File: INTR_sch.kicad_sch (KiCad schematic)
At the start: 1 part

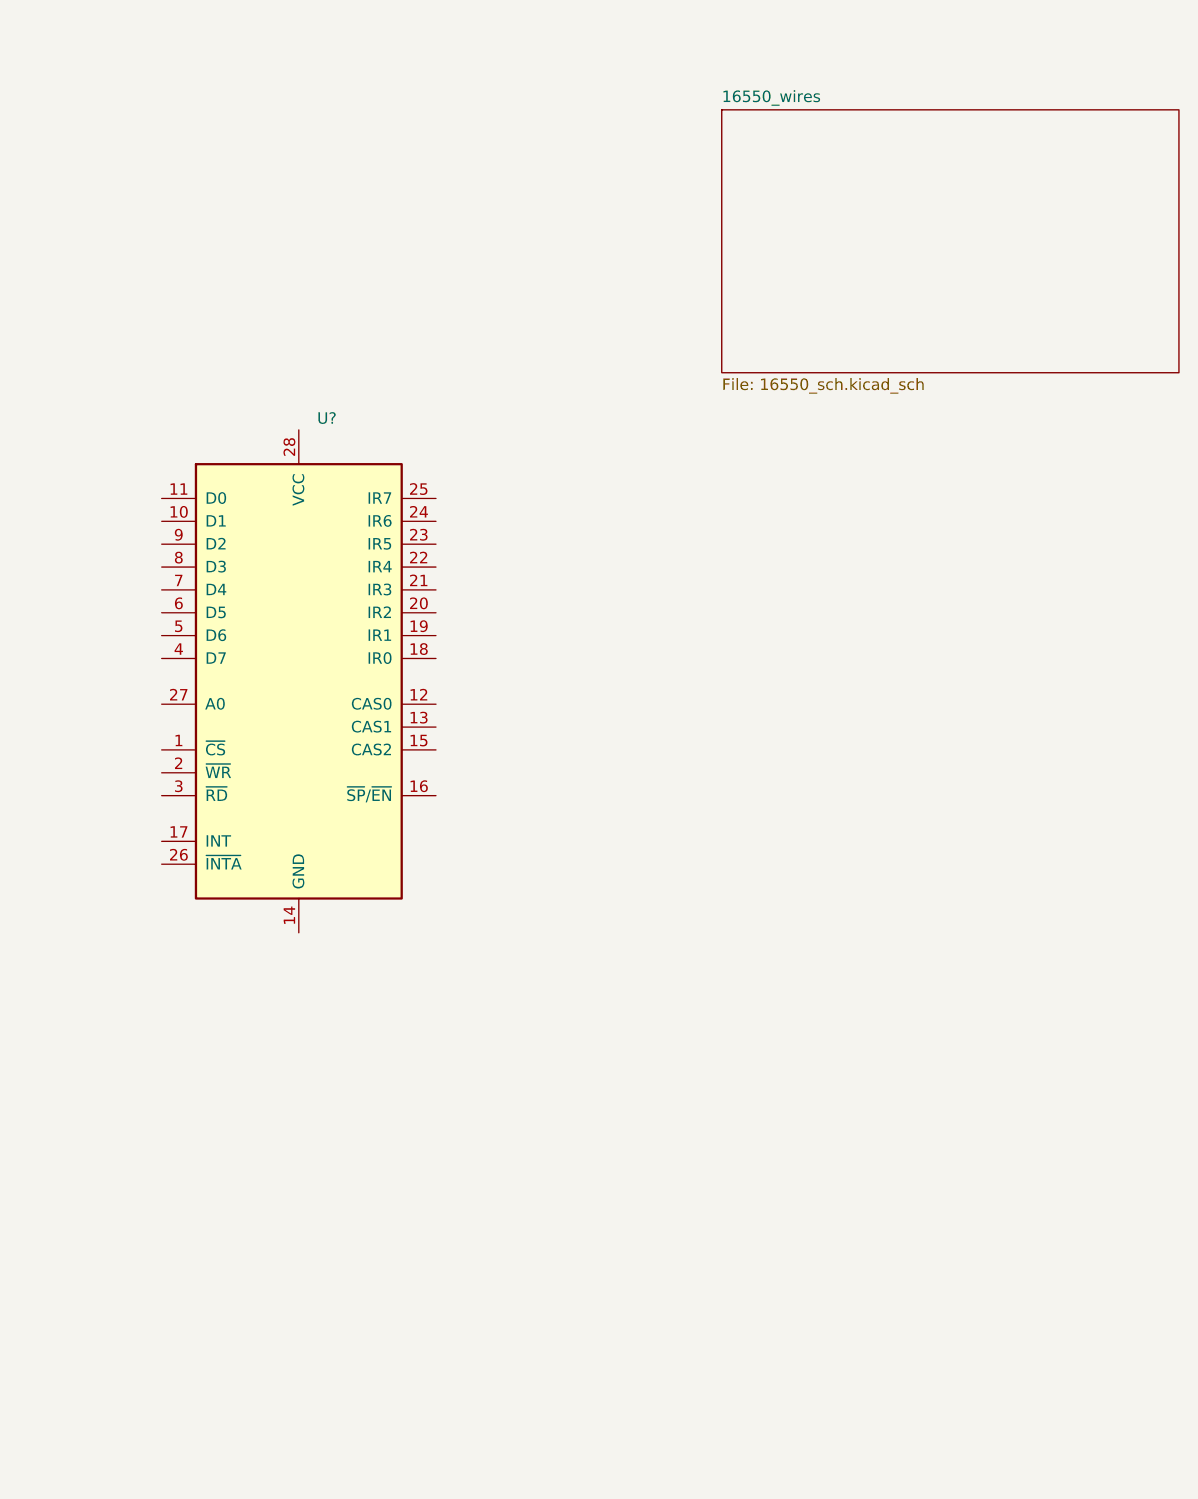
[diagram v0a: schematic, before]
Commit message: Wired the UART to the 8259A
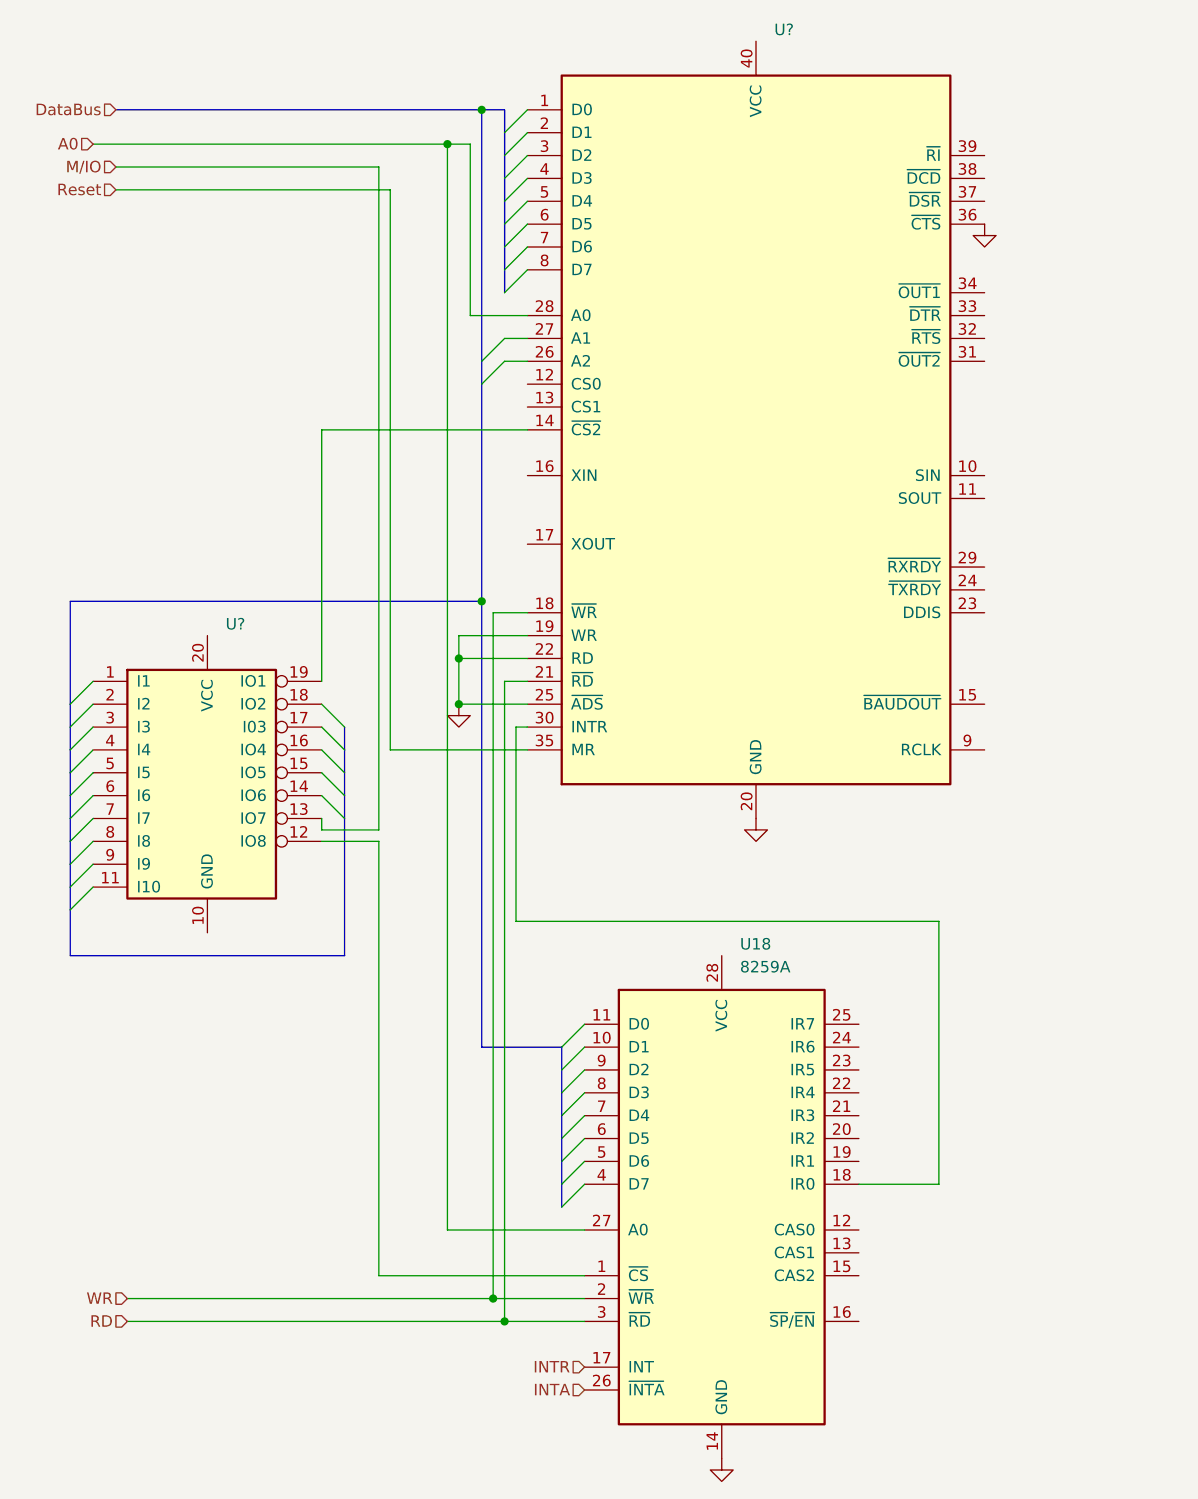
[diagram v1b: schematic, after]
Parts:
- added U?: (no value), symbol Interface_UART:16550
- added U?: (no value), symbol Logic_Programmable:PAL16L8
- U18: renamed from U?; value (none) -> 8259A; footprint (none) -> Package_DIP:DIP-28_W15.24mm
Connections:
- net at U18.1 (~{CS}): now also U?.12 (IO8)
- net GND: now reaches U18.14 (GND)
- net GND: now also U?.19 (WR), U?.20 (GND), U?.22 (RD), U?.25 (~{ADS}), U?.36 (~{CTS})
- net INTR: now reaches U18.17 (INT)
- net at U18.18 (IR0): now also U?.30 (INTR)
- net WR: now reaches U18.2 (~{WR})
- net WR: now also U?.18 (~{WR})
- net INTA: now reaches U18.26 (~{INTA})
- net A0: now reaches U18.27 (A0)
- net A0: now also U?.28 (A0)
- net RD: now reaches U18.3 (~{RD})
- net RD: now also U?.21 (~{RD})
- new net: U?.14 (~{CS2}), U?.19 (IO1)
- new net M/IO: U?.13 (IO7)
- new net Reset: U?.35 (MR)
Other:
- removed sheet 16550_wires
- moved on the sheet: U18

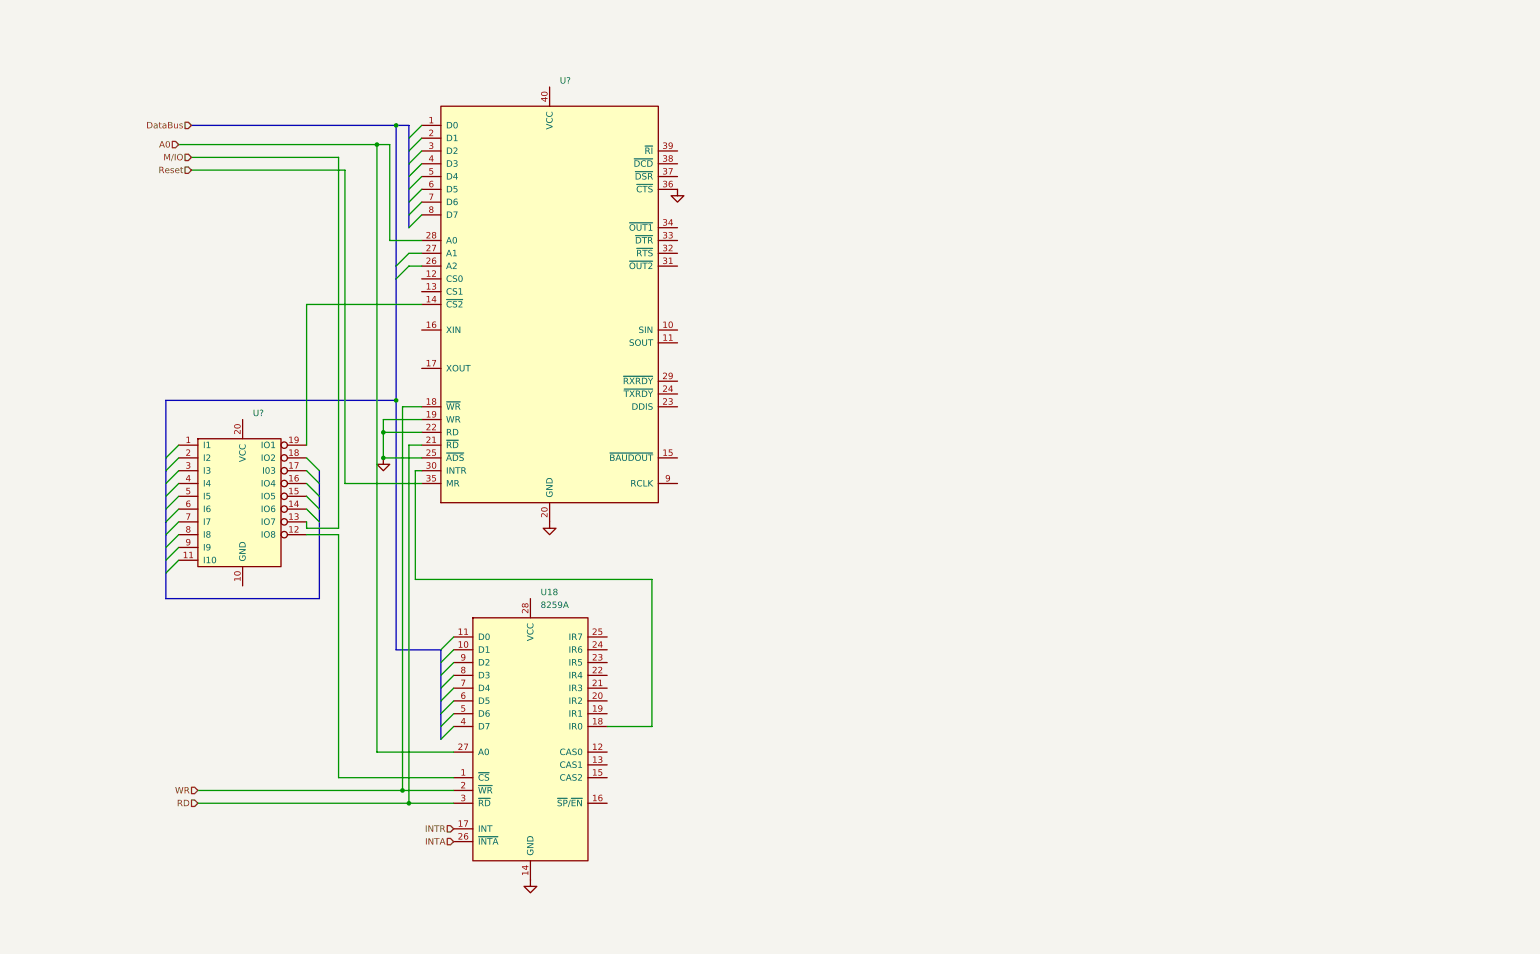
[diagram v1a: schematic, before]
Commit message: Wired up Decoding of 8255s, 8254, and 8279
Also fixed up the decoding for the 16550 and the 8259 as well as labeled all wires into/from the bus.
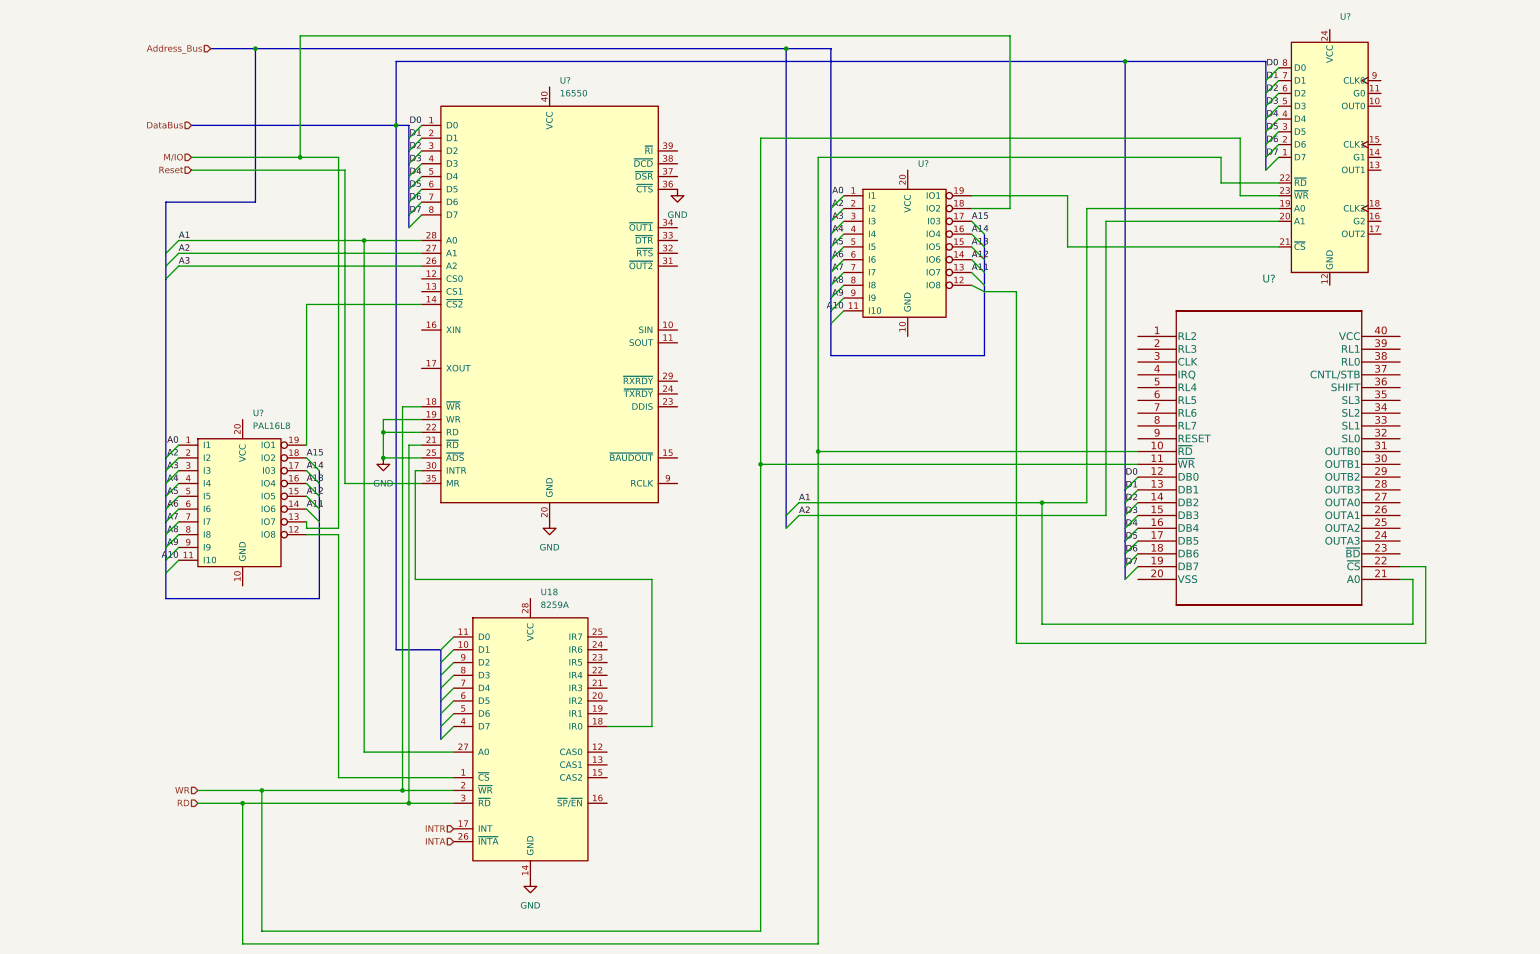
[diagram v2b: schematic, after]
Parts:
- added U?: (no value), symbol Logic_Programmable:PAL16L8
- added U?: (no value), symbol Timer:8254
- added U?: (no value), symbol pkd8279:pkd8279
- U?: value (none) -> 16550; footprint (none) -> Package_DIP:DIP-40_W15.24mm
- U?: value (none) -> PAL16L8
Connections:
- net A0: now also U?.1 (I1), U?.1 (I1); no longer U18.27 (A0), U?.28 (A0)
- net M/IO: now also U?.18 (IO2)
- net RD: now also U?.10 (~{RD}), U?.22 (~{RD})
- net WR: now also U?.11 (~{WR}), U?.23 (~{WR})
- net D0: now reaches U?.1 (D0)
- net D0: now also U?.12 (DB0), U?.8 (D0)
- net D1: now reaches U?.2 (D1)
- net D1: now also U?.13 (DB1), U?.7 (D1)
- net A3: now reaches U?.26 (A2)
- net A3: now also U?.3 (I3), U?.3 (I3)
- net A2: now reaches U?.27 (A1)
- net A2: now also U?.2 (I2), U?.2 (I2), U?.20 (A1)
- net D2: now reaches U?.3 (D2)
- net D2: now also U?.14 (DB2), U?.6 (D2)
- net D3: now reaches U?.4 (D3)
- net D3: now also U?.15 (DB3), U?.5 (D3)
- net D4: now reaches U?.5 (D4)
- net D4: now also U?.16 (DB4), U?.4 (D4)
- net D5: now reaches U?.6 (D5)
- net D5: now also U?.17 (DB5), U?.3 (D5)
- net D6: now reaches U?.7 (D6)
- net D6: now also U?.18 (DB6), U?.2 (D6)
- net D7: now reaches U?.8 (D7)
- net D7: now also U?.1 (D7), U?.19 (DB7)
- net A10: now reaches U?.11 (I10)
- net A10: now also U?.11 (I10)
- net A11: now reaches U?.14 (IO6)
- net A11: now also U?.13 (IO7)
- net A12: now reaches U?.15 (IO5)
- net A12: now also U?.14 (IO6)
- net A13: now reaches U?.16 (IO4)
- net A13: now also U?.15 (IO5)
- net A14: now reaches U?.17 (I03)
- net A14: now also U?.16 (IO4)
- net A15: now reaches U?.18 (IO2)
- net A15: now also U?.17 (I03)
- net A4: now reaches U?.4 (I4)
- net A4: now also U?.4 (I4)
- net A5: now reaches U?.5 (I5)
- net A5: now also U?.5 (I5)
- net A6: now reaches U?.6 (I6)
- net A6: now also U?.6 (I6)
- net A7: now reaches U?.7 (I7)
- net A7: now also U?.7 (I7)
- net A8: now reaches U?.8 (I8)
- net A8: now also U?.8 (I8)
- net A9: now reaches U?.9 (I9)
- net A9: now also U?.9 (I9)
- new net: U?.12 (IO8), U?.22 (~{CS})
- new net: U?.19 (IO1), U?.21 (~{CS})
- new net A1: U18.27 (A0), U?.19 (A0), U?.21 (A0), U?.28 (A0)

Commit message: Wired the max235 and DSUB9
We will double check the wiring tomorrow. Also added the data bus
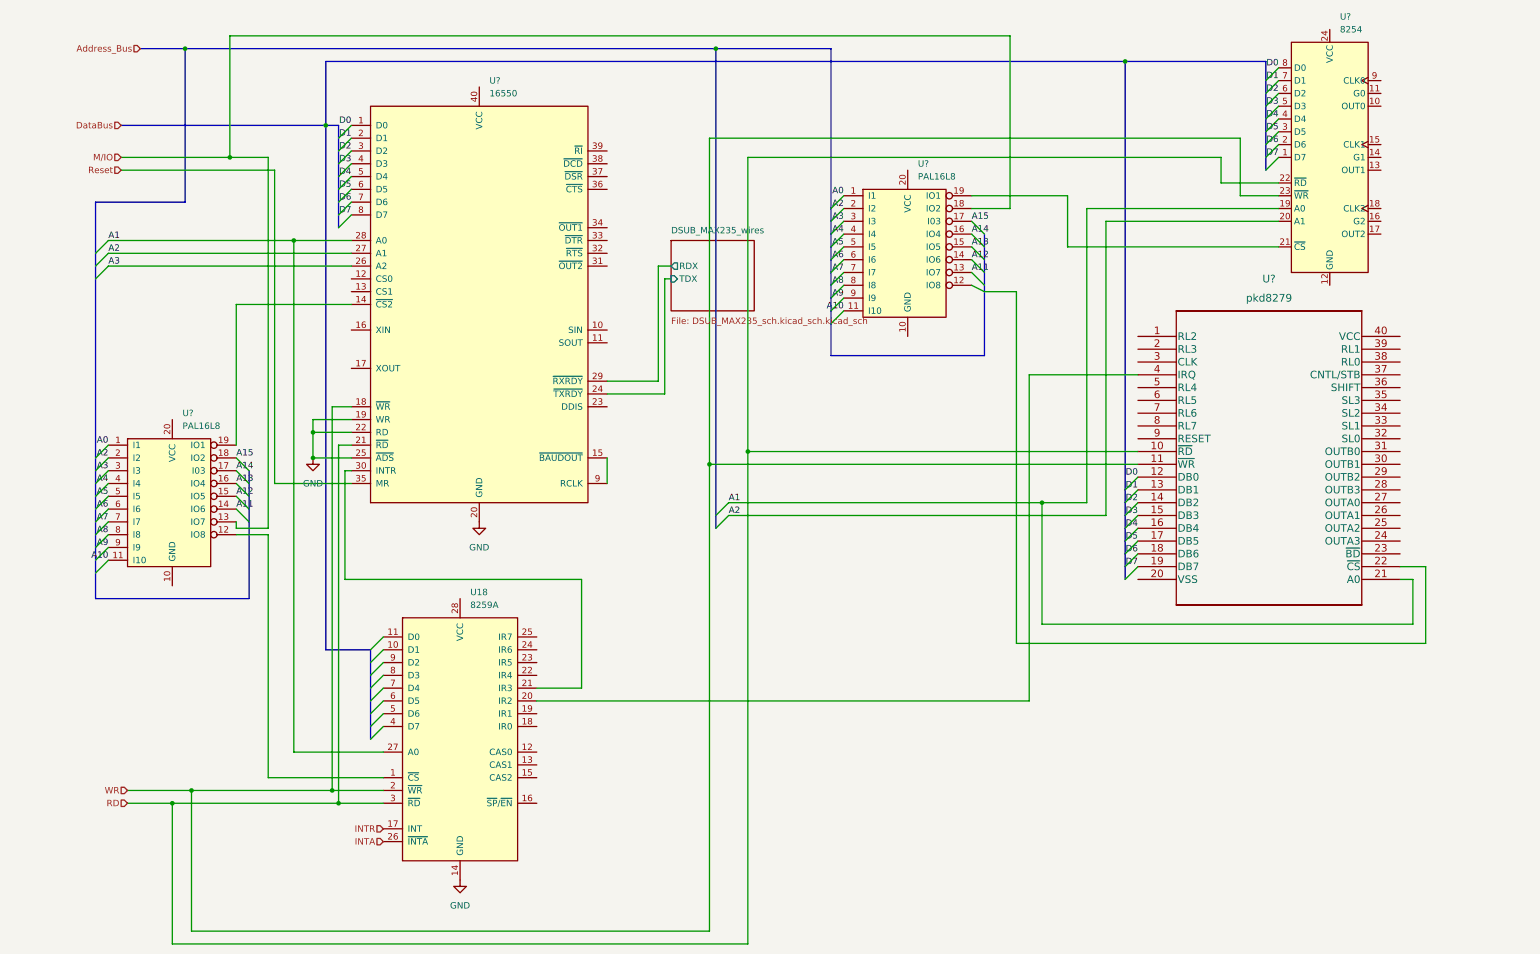
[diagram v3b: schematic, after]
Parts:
- U?: value (none) -> PAL16L8
- U?: value (none) -> 8254; footprint (none) -> Package_DIP:DIP-24_W15.24mm
- U?: value (none) -> pkd8279; footprint (none) -> pkd8279
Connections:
- net GND: no longer U?.36 (~{CTS})
- net at U?.15 (~{BAUDOUT}): now also U?.9 (RCLK)
- net DSUB_MAX235_wires/TDX: now reaches U?.24 (~{TXRDY})
- net DSUB_MAX235_wires/RDX: now reaches U?.29 (~{RXRDY})
- net at U?.30 (INTR): now also U18.21 (IR3); no longer U18.18 (IR0)
- net at U18.20 (IR2): now also U?.4 (IRQ)
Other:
- added sheet DSUB_MAX235_wires (DSUB_MAX235_sch.kicad_sch.kicad_sch)
- moved on the sheet: U18, U?

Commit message: Added the databus
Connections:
- net at U?.15 (~{BAUDOUT}): no longer U?.9 (RCLK)
- net PCLK: now reaches U?.3 (CLK)
- net PCLK: now also U?.9 (RCLK)
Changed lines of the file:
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@@
   (junction (at 67.31 167.64) (diameter 0) (color 0 0 0 0)
   )
+  (junction (at 181.61 104.14) (diameter 0) (color 0 0 0 0)
+  )
   (junction (at 34.29 167.64) (diameter 0) (color 0 0 0 0)
   )
@@
     (stroke (width 0) (type default) (color 0 0 0 0))
   )
+  (wire (pts (xy 226.06 80.01) (xy 181.61 80.01))
+    (stroke (width 0) (type default) (color 0 0 0 0))
+  )
   (bus (pts (xy 19.05 48.26) (xy 36.83 48.26))
     (stroke (width 0) (type default) (color 0 0 0 0))
@@
     (stroke (width 0) (type default) (color 0 0 0 0))
   )
+  (wire (pts (xy 120.65 104.14) (xy 181.61 104.14))
+    (stroke (width 0) (type default) (color 0 0 0 0))
+  )
   (bus (pts (xy 223.52 107.95) (xy 223.52 110.49))
     (stroke (width 0) (type default) (color 0 0 0 0))
@@
     (stroke (width 0) (type default) (color 0 0 0 0))
   )
+  (wire (pts (xy 181.61 80.01) (xy 181.61 104.14))
+    (stroke (width 0) (type default) (color 0 0 0 0))
+  )
   (bus (pts (xy 73.66 137.16) (xy 64.77 137.16))
     (stroke (width 0) (type default) (color 0 0 0 0))
@@
     (stroke (width 0) (type default) (color 0 0 0 0))
   )
-  (wire (pts (xy 120.65 99.06) (xy 120.65 104.14))
-    (stroke (width 0) (type default) (color 0 0 0 0))
-  )
   (bus (pts (xy 142.24 17.78) (xy 165.1 17.78))
     (stroke (width 0) (type default) (color 0 0 0 0))
@@
   )
   (wire (pts (xy 115.57 144.78) (xy 106.68 144.78))
+    (stroke (width 0) (type default) (color 0 0 0 0))
+  )
+  (wire (pts (xy 181.61 104.14) (xy 181.61 121.92))
     (stroke (width 0) (type default) (color 0 0 0 0))
   )
@@
     (effects (font (size 1.27 1.27)) (justify right))
   )
+  (hierarchical_label "PCLK" (shape input) (at 181.61 121.92 0)
+    (effects (font (size 1.27 1.27)) (justify left))
+  )
   (hierarchical_label "RD" (shape input) (at 25.4 167.64 180)
